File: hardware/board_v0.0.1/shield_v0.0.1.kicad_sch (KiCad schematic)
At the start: 17 parts, among them IC1 BQ25172DSGR, IC2 TPS2117DRLR, J1 USB_C_Receptacle_PowerOnly_6P, U1 STM32L053R8Tx

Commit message: Design improvements
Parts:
- removed U1: STM32L053R8Tx, Package_QFP:LQFP-64_10x10mm_P0.5mm, symbol MCU_ST_STM32L0:STM32L053R8Tx
- added C10: 10u, symbol Device:C
- added C11, C12, C13: 10n, symbol Device:C
- added C14, C3: 1u, symbol Device:C
- added C4, C5, C6, C9: 100n, symbol Device:C
- added C8: 33n, symbol Device:C
- added D2: LED, symbol Device:LED
- added IC3: ADP160AUJZ-3.3-R7, SOT95P280X100-5N, symbol ADP160AUJZ-3_3-R7:ADP160AUJZ-3.3-R7
- added J2: Conn_02x05_Odd_Even, symbol Connector_Generic:Conn_02x05_Odd_Even
- added R10, R12, R14: 10k, symbol Device:R
- added R11: 22k, symbol Device:R
- added R13: 2k2, symbol Device:R
- added U2: nRF24L01P, Package_DFN_QFN:QFN-20-1EP_4x4mm_P0.5mm_EP2.5x2.5mm, symbol RF:nRF24L01P
- added U3: STM32L071K_B-Z_Tx, Package_QFP:LQFP-32_7x7mm_P0.8mm, symbol MCU_ST_STM32L0:STM32L071K_B-Z_Tx
- added Y1: Crystal_GND24, symbol Device:Crystal_GND24
- R1: value R -> 600
- R2, R7: value 18k -> 15k
- R8: value 18k -> 1k
- R9: value 18k -> 2k
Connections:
- net +5V: now also IC2.5 (MODE), R14.1
- net GND: now also IC1.4 (GND_1), C10.2, C11.2, C12.2, C13.2, C14.2, C3.2, C4.2, C5.2, C6.2, C8.2, C9.2, IC3.2 (GND), J2.3 (Pin_3), J2.5 (Pin_5), J2.9 (Pin_9), R10.2, R12.2, R13.2, U2.14 (VSS), U2.17 (VSS), U2.20 (VSS), U2.8 (VSS), U3.16 (VSS), U3.32 (VSS)
- net POWER_STAT: now reaches IC2.8 (ST)
- net POWER_STAT: now also R14.2
- net at IC1.3 (TS): now also R10.1
- net VCC: no longer names the net of IC2.7 (VOUT_2)
- net VCC: now also IC3.1 (VIN), IC3.3 (EN)
- new net: D2.1 (K), R13.1
- new net: D2.2 (A), U3.19 (PA9)
- new net: C8.1, U2.19 (DVDD)
- new net: R11.2, U2.16 (IREF)
- new net: R12.1, U3.31 (BOOT0)
- new net +3.3V: C10.1, C11.1, C12.1, C13.1, C14.1, C3.1, C4.1, C5.1, C6.1, IC3.5 (VOUT), J2.1 (Pin_1), R11.1, U2.15 (VDD), U2.18 (VDD), U2.7 (VDD), U3.1 (VDD), U3.17 (VDD), U3.5 (VDDA)
- new net ADC_IN0: U3.6 (PA0)
- new net I2C1_SCL: U3.30 (PB7)
- new net I2C1_SDA: U3.29 (PB6)
- new net NRF_CE: U2.1 (CE)
- new net NRF_IRQ: U2.6 (IRQ)
- new net NRST: C9.1, J2.10 (Pin_10), U3.4 (NRST)
- new net SPI1_MISO: U2.5 (MISO), U3.12 (PA6)
- new net SPI1_MOSI: U2.4 (MOSI), U3.13 (PA7)
- new net SPI1_SCK: U2.3 (SCK), U3.11 (PA5)
- new net SWCLK: J2.4 (Pin_4), U3.24 (PA14)
- new net SWDIO: J2.2 (Pin_2), U3.23 (PA13)
- new net USART1_RX: U3.10 (PA4)
- new net USART1_TX: U3.9 (PA3)
- no-connect marks 1 -> 4
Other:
- note added: "Battery charging and power section"
- note added: "MCU"
- note added: "NRF24 Trasciever"
- note added: "SWD Connector"
- note added: "USB Connector"
- moved on the sheet: BT1, C1, C2, D1, IC1, IC2, J1, R1, R2, R3, R4, R5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

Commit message: Updated schematics
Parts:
- removed BT1: Battery, symbol Device:Battery
- removed U3: STM32L071K_B-Z_Tx, Package_QFP:LQFP-32_7x7mm_P0.8mm, symbol MCU_ST_STM32L0:STM32L071K_B-Z_Tx
- removed Y1: Crystal_GND24, symbol Device:Crystal_GND24
- added C15, C7: 22p, symbol Device:C
- added C16: 2n2, symbol Device:C
- added C17: 4p7, symbol Device:C
- added J3: SMA, symbol Connector:Conn_Coaxial
- added J4, J6, J8: Conn_01x02_Pin, symbol Connector:Conn_01x02_Pin
- added J5: Conn_01x08_Pin, symbol Connector:Conn_01x08_Pin
- added J7: Conn_02x05_Odd_Even, symbol Connector_Generic:Conn_02x05_Odd_Even
- added L1: 8n2, symbol Device:L
- added L2: 3n9, symbol Device:L
- added L3: 2n7, symbol Device:L
- added R15: 22k, symbol Device:R
- added U3: STM32L071KBT6, Package_QFP:LQFP-32_7x7mm_P0.8mm, symbol MCU_ST_STM32L0:STM32L071KBTx
- added Y1: 16MHz, symbol Device:Crystal
- C10: value 10u -> 10n
- C11: value 10n -> 1n
- C12: value 10n -> 1p5
- C13: value 10n -> 1p
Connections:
- net +3.3V: now also J7.10 (Pin_10), U3.1 (VDD), U3.17 (VDD), U3.5 (VDDA); no longer C12.1, C13.1
- net ADC_IN0: now also J7.2 (Pin_2), U3.6 (PA0)
- net GND: now also C15.2, C16.2, C17.2, C7.2, J5.1 (Pin_1), J7.7 (Pin_7), J7.9 (Pin_9), J8.1 (Pin_1), U3.16 (VSS), U3.32 (VSS); no longer C12.2
- net I2C1_SCL: now also J4.2 (Pin_2), U3.29 (PB6)
- net I2C1_SDA: now also J4.1 (Pin_1), U3.30 (PB7)
- net NRF_ANT1: now also U2.12 (ANT1), L1.2, L3.1
- net NRF_ANT2: now also U2.13 (ANT2), L1.1, L2.1
- net NRF_VDD_PA: now also U2.11 (VDD_PA), C16.1, C17.1, L3.2
- net NRST: now also U3.4 (NRST)
- net SPI1_MISO: now also U3.12 (PA6)
- net SPI1_MOSI: now also U3.13 (PA7)
- net SPI1_SCK: now also U3.11 (PA5)
- net SWCLK: now also U3.24 (PA14)
- net SWDIO: now also U3.23 (PA13)
- net USART1_RX: now also J6.2 (Pin_2), U3.20 (PA10)
- net USART1_TX: now also J6.1 (Pin_1), U3.19 (PA9)
- net at D2.2 (A): now also U3.18 (PA8)
- net BAT: now reaches C2.1, IC1.8 (OUT), IC2.6 (VIN2)
- net at U2.10 (XC1): now also C7.1, R15.1, Y1.1
- net at U2.9 (XC2): now also C15.1, R15.2, Y1.2
- net at R12.1: now also U3.31 (BOOT0)
- new net: C12.1, L2.2
- new net: C12.2, J3.1 (In)
- new net: C13.1, J3.2 (Ext)
- new net BAT+: J8.2 (Pin_2)
- new net PA1: J7.4 (Pin_4), U3.7 (PA1)
- new net PA11: J7.5 (Pin_5), U3.21 (PA11)
- new net PA15: J7.1 (Pin_1), U3.25 (PA15)
- new net PA2: J7.6 (Pin_6), U3.8 (PA2)
- new net PA22: J7.3 (Pin_3), U3.22 (PA12)
- new net PA3: J7.8 (Pin_8), U3.9 (PA3)
- new net PA4: U3.10 (PA4)
- new net PB0: J5.6 (Pin_6), U3.14 (PB0)
- new net PB1: J5.5 (Pin_5), U3.15 (PB1)
- new net PB3: J5.4 (Pin_4), U3.26 (PB3)
- new net PB4: J5.3 (Pin_3), U3.27 (PB4)
- new net PB5: J5.2 (Pin_2), U3.28 (PB5)
- new net PC14: J5.8 (Pin_8), U3.2 (PC14)
- new net PC15: J5.7 (Pin_7), U3.3 (PC15)
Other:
- note added: "Connectors"
- note added: "SMA connector"
- moved on the sheet: C1, C10, C11, C14, C2, C3, C4, C5, C6, C8, C9, D1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

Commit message: Added footprints
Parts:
- removed J4: Conn_01x02_Pin, symbol Connector:Conn_01x02_Pin
- removed J5: Conn_01x08_Pin, symbol Connector:Conn_01x08_Pin
- removed J7: Conn_02x05_Odd_Even, symbol Connector_Generic:Conn_02x05_Odd_Even
- added C18, C19, C20: 10n, Capacitor_SMD:C_0805_2012Metric, symbol Device:C
- added J4: I2C_CONNECTOR, Connector_PinHeader_2.54mm:PinHeader_1x04_P2.54mm_Vertical, symbol Connector:Conn_01x04_Pin
- added J5: ADC_CONNECTOR, Connector_PinHeader_2.54mm:PinHeader_1x04_P2.54mm_Vertical, symbol Connector:Conn_01x04_Pin
- added J9: GPS_CONNECTOR, Connector_PinHeader_2.54mm:PinHeader_1x04_P2.54mm_Vertical, symbol Connector:Conn_01x04_Pin
- added Q1, Q2, Q3: PMOS, Package_TO_SOT_SMD:SOT-23, symbol Simulation_SPICE:PMOS
- added R16: 10k, Resistor_SMD:R_0805_2012Metric, symbol Device:R
- added SW1: SW_SPDT, symbol Switch:SW_SPDT
- C1, C10, C11, C12, C13, C14, C15, C16, C17, C2, C3, C4, C5, C6, C7, C8, C9: footprint (none) -> Capacitor_SMD:C_0805_2012Metric
- J2: value Conn_02x05_Odd_Even -> SWD_CONNECTOR; footprint (none) -> Connector_PinHeader_2.54mm:PinHeader_2x05_P2.54mm_Vertical
- J3: value SMA -> UFL; footprint (none) -> Connector_Coaxial:U.FL_Molex_MCRF_73412-0110_Vertical
- J6: value Conn_01x02_Pin -> VCC_CONNECTOR; footprint (none) -> Connector_PinHeader_2.54mm:PinHeader_1x02_P2.54mm_Vertical
- J8: value Conn_01x02_Pin -> BATTERY_CONNECTOR; footprint (none) -> Connector_PinHeader_2.54mm:PinHeader_1x02_P2.54mm_Vertical
- L1, L2, L3: footprint (none) -> Inductor_SMD:L_0805_2012Metric
- R1, R10, R11, R12, R13, R14, R15, R2, R3, R4, R5, R6, R7, R8, R9: footprint (none) -> Resistor_SMD:R_0805_2012Metric
- Y1: footprint (none) -> Crystal:Crystal_HC52-U_Vertical
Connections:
- net PB0 is gone; now on net PA15: U3.14 (PB0)
- net PB1 is gone; now on net PA15: U3.15 (PB1)
- net PB3 is gone; now on net PA15: U3.26 (PB3)
- net PB4 is gone; now on net NRF_CE: U3.27 (PB4)
- net PB5 is gone; now on net NRF_IRQ: U3.28 (PB5)
- net PC14 is gone; now on net PA15: U3.2 (PC14)
- net PC15 is gone; now on net PA15: U3.3 (PC15)
- net +3.3V: now also J6.1 (Pin_1), Q1.3 (S), Q2.3 (S), Q3.3 (S)
- net +5V: now also C19.1
- net ADC_IN0: now also J5.1 (Pin_1)
- net BAT: now also C18.1, SW1.2 (B); no longer IC2.6 (VIN2)
- net GND: now also J6.2 (Pin_2), C18.2, C19.2, C20.2, J4.3 (Pin_3), J5.3 (Pin_3), J9.3 (Pin_3), R16.2, SW1.3 (C)
- net I2C1_SCL: now also J4.2 (Pin_2)
- net I2C1_SDA: now also J4.1 (Pin_1)
- net PA11: now also Q1.2 (G)
- net PA15: now also R16.1
- net at J1.S1 (SHIELD), R3.1: now also C20.1
- net PA1 renamed ADC_IN1
- net ADC_IN1: now also J5.2 (Pin_2)
- net PA2 renamed LPUART_TX
- net LPUART_TX: now also J9.1 (Pin_1)
- net PA22 renamed PA12
- net PA12: now also Q3.2 (G)
- net PA3 renamed LPUART_RX
- net LPUART_RX: now also J9.2 (Pin_2)
- net USART1_RX renamed PA10
- net PA10: now also Q2.2 (G); no longer J6.2 (Pin_2)
- net USART1_TX renamed PA9
- net PA9: no longer J6.1 (Pin_1)
- new net: J9.4 (Pin_4), Q1.1 (D)
- new net: J4.4 (Pin_4), Q2.1 (D)
- new net: J5.4 (Pin_4), Q3.1 (D)
- new net ON/OFF_OUT: IC2.6 (VIN2), SW1.1 (A)
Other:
- moved on the sheet: C1, C14, C2, D1, IC1, IC2, IC3, J1, J8, R1, R10, R14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

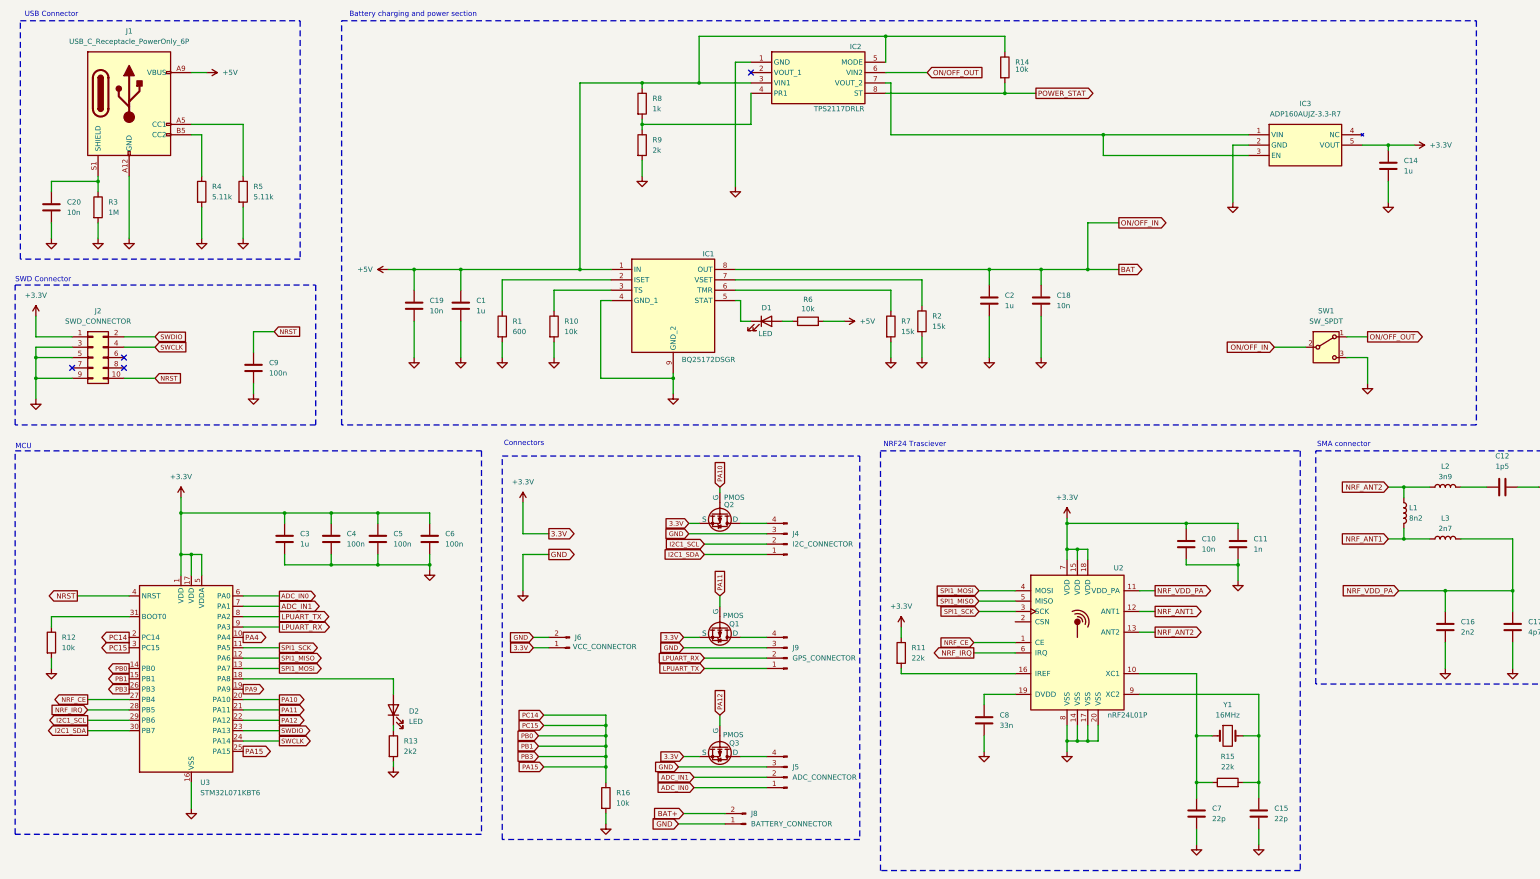
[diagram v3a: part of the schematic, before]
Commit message: Added footprints
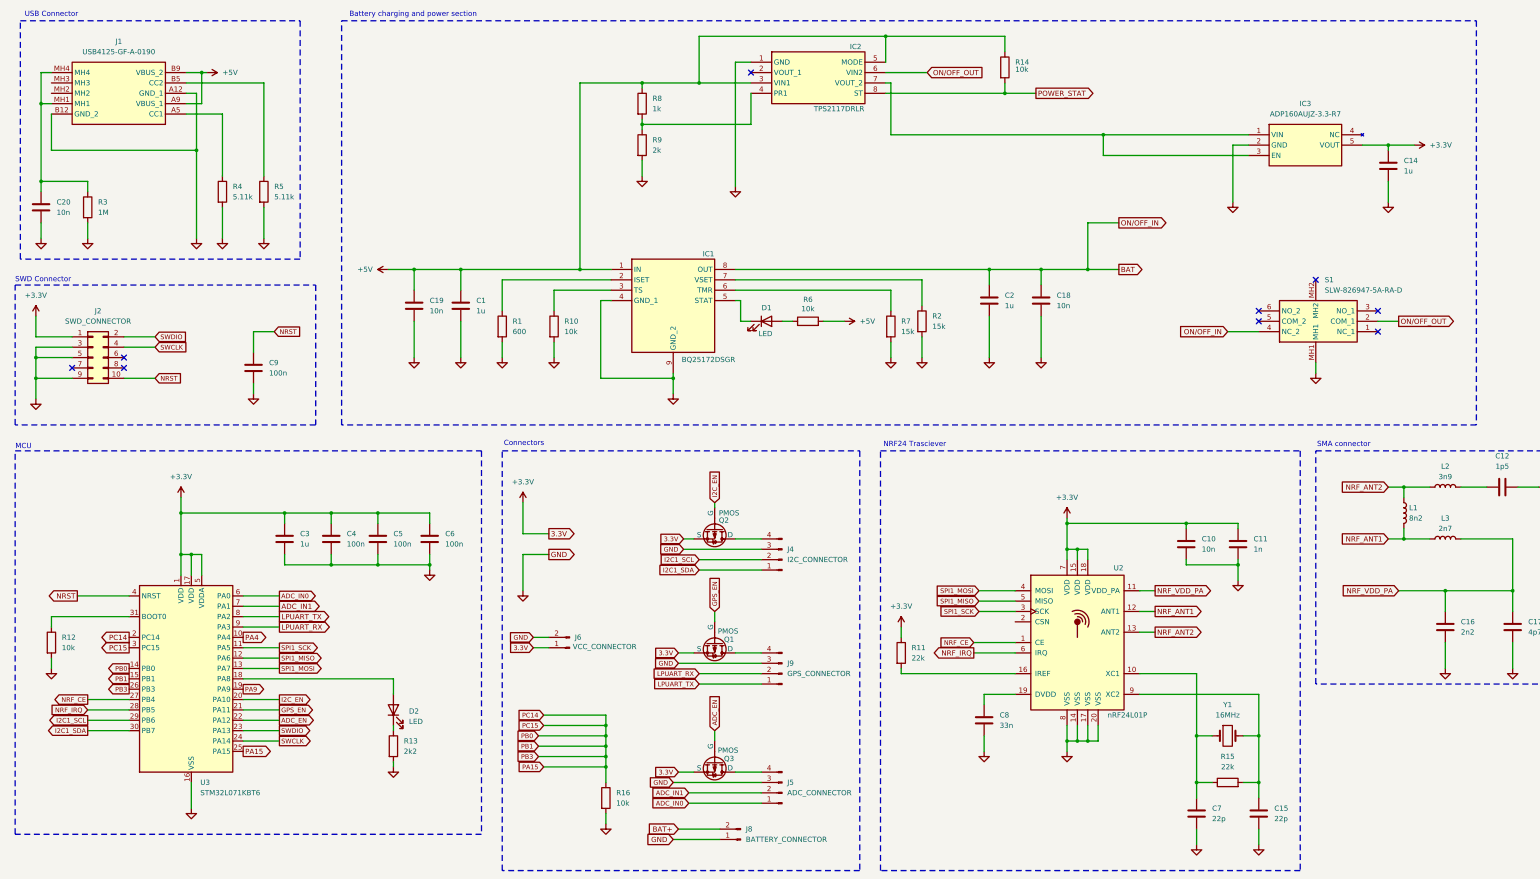
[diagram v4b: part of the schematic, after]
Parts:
- removed J1: USB_C_Receptacle_PowerOnly_6P, symbol Connector:USB_C_Receptacle_PowerOnly_6P
- removed SW1: SW_SPDT, symbol Switch:SW_SPDT
- added J1: USB4125-GF-A-0190, USB4125GFA0190, symbol USB4125-GF-A-0190:USB4125-GF-A-0190
- added S1: SLW-826947-5A-RA-D, SLW-826947-5A-RA-D:SLW8269475ARAD, symbol SLW-826947-5A-RA-D:SLW-826947-5A-RA-D
- D1, D2: footprint (none) -> nasze:nasz_zajebisty_led
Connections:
- net +5V: now also J1.A9 (VBUS_1), J1.B9 (VBUS_2)
- net BAT: now also S1.4 (NC_2)
- net GND: now also J1.A12 (GND_1), J1.B12 (GND_2), S1.MH1
- net ON/OFF_OUT: now also S1.2 (COM_1)
- net at R5.1: now also J1.B5 (CC2)
- net at R4.1: now also J1.A5 (CC1)
- net at C20.1, R3.1: now also J1.MH1, J1.MH4
- net PA10 renamed I2C_EN
- net PA11 renamed GPS_EN
- net PA12 renamed ADC_EN
- no-connect marks 4 -> 9
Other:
- moved on the sheet: C20, J4, J5, J8, J9, Q1, Q2, Q3, R3, R4, R5

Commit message: Minor changer
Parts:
- S1: value SLW-826947-5A-RA-D -> ON/OFF_SWITCH
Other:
- note added: "Sensor connectors"
- note removed: "Connectors"
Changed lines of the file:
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@@
 		)
 	)
-	(text "Connectors"
+	(text "Sensor connectors"
 		(exclude_from_sim no)
-		(at 141.224 122.682 0)
+		(at 145.034 122.682 0)
 		(effects
 			(font
@@
 			)
 		)
-		(property "Value" "SLW-826947-5A-RA-D"
+		(property "Value" "ON/OFF_SWITCH"
 			(at 337.4741 85.09 90)
 			(effects
